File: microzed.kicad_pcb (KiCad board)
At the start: 10 copper layers, 19 x 19 mm, 329 parts, among them IC1 XC7Z020-1CLG484C, IC2 RTL8211E-VL-CG, J1 640456-3, J2 10104111-0001LF, J3 L829-1J1T-43, J4 Micro_SD_Card_Det_Hirose_DM3AT, J5 10104111-0001LF, J6 BSH-090-01-X-D-A, J7 BSH-090-01-X-D-A, Q1 MMBT3904, Q2 MMBT3904, SW1 SW_Push, U1 TLV62130RGTR, U10 MT41K256M16TW, U11 MT25QL128ABA8E12-1SIT, U12 USB3320C-EZK, U13 ASDMB-24.000MHZ-LC-T, U14 ASDMB-25.000MHZ-LC-T, U15 TXS02612RTWR, U16 CP2104-F03-GM, U2 TLV62130RGTR, U3 TLV62130RGTR, U4 TLV62130RGTR, U5 TLV62130RGTR, U6 ASDMB-33.333MHZ-LC-T, U7 TPS51206DSQR, U8 REF3012, U9 MT41K256M16TW

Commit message: add zone for GND
Signed-off-by: Yi Qingliang <niqingliang2003@gmail.com>
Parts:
- moved R19 0.09 mm to (-37.9, 23.4)
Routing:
- net GND: track 11.9 -> 3.14 mm
- net Net-(L4-Pad1): track 3.99 -> 0.00 mm
- net V3V3: track 6.68 -> 9.95 mm, vias 3 -> 2
- net /pwrcvt/PG_1V35: track 0.00 -> 1.85 mm, vias 0 -> 1
- net (no net): vias 0 -> 1
- added copper zone on In1.Cu.GND, net GND
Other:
- board size 19 x 19 mm -> 20.3 x 19 mm
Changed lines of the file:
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@@
     (thickness 1.6)
     (drawings 4)
-    (tracks 57)
+    (tracks 41)
     (zones 0)
     (modules 329)
@@
   (layers
     (0 F.Cu signal)
-    (1 In1.Cu power)
-    (2 In2.Cu signal)
-    (3 In3.Cu signal)
-    (4 In4.Cu power)
-    (5 In5.Cu power)
-    (6 In6.Cu signal)
-    (7 In7.Cu signal)
-    (8 In8.Cu power)
+    (1 In1.Cu.GND power)
+    (2 In2.Cu.signal signal)
+    (3 In3.Cu.signal signal)
+    (4 In4.Cu.VDD power)
+    (5 In5.Cu.GND power)
+    (6 In6.Cu.signal signal)
+    (7 In7.Cu.signal signal)
+    (8 In8.Cu.VCC power)
     (31 B.Cu signal)
     (32 B.Adhes user)
@@
     (trace_clearance 0.2)
     (zone_clearance 0.508)
-    (zone_45_only no)
+    (zone_45_only yes)
     (trace_min 0.2)
     (via_size 0.8)
@@
   )
   (module Resistor_SMD:R_0402_1005Metric (layer F.Cu)
-    (at -37.823 23.368)
+    (at -37.9095 23.368)
     (descr "Resistor SMD 0402 (1005 Metric), square (rectangular) end terminal, IPC_7351 nominal, (Body size source: http://www.tortai-tech.com/upload/download/2011102023233369053.pdf), generated with kicad-footprint-generator")
     (tags resistor)
@@
     )
   )
-  (gr_line (start -33.655 15.24) (end -33.655 34.29) (layer Edge.Cuts) (width 0.05))
-  (gr_line (start -52.705 15.24) (end -33.655 15.24) (layer Edge.Cuts) (width 0.05))
-  (gr_line (start -52.705 34.29) (end -52.705 15.24) (layer Edge.Cuts) (width 0.05))
-  (gr_line (start -33.655 34.29) (end -52.705 34.29) (layer Edge.Cuts) (width 0.05))
+  (gr_line (start -33.02 15.24) (end -33.02 34.29) (layer Edge.Cuts) (width 0.05))
+  (gr_line (start -53.34 15.24) (end -33.02 15.24) (layer Edge.Cuts) (width 0.05))
+  (gr_line (start -53.34 34.29) (end -53.34 15.24) (layer Edge.Cuts) (width 0.05))
+  (gr_line (start -33.02 34.29) (end -53.34 34.29) (layer Edge.Cuts) (width 0.05))
+  (via (at -41.91 25.908) (size 0.5) (drill 0.3) (layers F.Cu B.Cu) (net 0))
+  (via (at -39.37 29.21) (size 0.5) (drill 0.3) (layers F.Cu B.Cu) (net 9))
   (via (at -46.482 21.336) (size 0.5) (drill 0.3) (layers F.Cu B.Cu) (net 1))
   (via (at -47.498 22.352) (size 0.5) (drill 0.3) (layers F.Cu B.Cu) (net 1))
   (via (at -37.338 22.352) (size 0.5) (drill 0.3) (layers F.Cu B.Cu) (net 1))
-  (via (at -39.878 22.86) (size 0.5) (drill 0.3) (layers F.Cu B.Cu) (net 350))
-  (via (at -43.688 24.892) (size 0.5) (drill 0.3) (layers F.Cu B.Cu) (net 1))
-  (via (at -43.18 24.384) (size 0.5) (drill 0.3) (layers F.Cu B.Cu) (net 1))
+  (via (at -43.688 24.765) (size 0.5) (drill 0.3) (layers F.Cu B.Cu) (net 1))
+  (via (at -43.18 24.301) (size 0.5) (drill 0.3) (layers F.Cu B.Cu) (net 1))
   (via (at -43.688 23.876) (size 0.5) (drill 0.3) (layers F.Cu B.Cu) (net 1))
   (via (at -42.672 23.876) (size 0.5) (drill 0.3) (layers F.Cu B.Cu) (net 1))
-  (via (at -42.672 24.892) (size 0.5) (drill 0.3) (layers F.Cu B.Cu) (net 1))
-  (segment (start -42.43 25.08) (end -42.545 24.965) (width 0.25) (layer F.Cu) (net 1))
-  (segment (start -42.43 25.5925) (end -42.43 25.08) (width 0.25) (layer F.Cu) (net 1))
-  (segment (start -42.93 25.5925) (end -42.93 25.015) (width 0.25) (layer F.Cu) (net 1))
-  (segment (start -43.43 22.6675) (end -43.43 23.88) (width 0.25) (layer F.Cu) (net 1))
-  (segment (start -42.93 22.6675) (end -42.93 23.88) (width 0.25) (layer F.Cu) (net 1))
-  (segment (start -44.473 21.336) (end -43.411 21.336) (width 0.25) (layer F.Cu) (net 1))
-  (segment (start -43.43 22.9215) (end -43.43 21.594) (width 0.25) (layer F.Cu) (net 1))
-  (segment (start -43.93 22.9215) (end -43.93 23.434) (width 0.25) (layer F.Cu) (net 1))
+  (via (at -42.672 24.765) (size 0.5) (drill 0.3) (layers F.Cu B.Cu) (net 1))
   (segment (start -37.338 23.368) (end -37.338 22.352) (width 0.25) (layer F.Cu) (net 1))
   (segment (start -46.482 22.398) (end -46.482 21.336) (width 0.25) (layer F.Cu) (net 1))
@@
   (segment (start -46.482 22.398) (end -47.452 22.398) (width 0.25) (layer F.Cu) (net 1))
   (segment (start -42.93 27.9185) (end -42.9515 27.94) (width 0.25) (layer F.Cu) (net 1))
-  (segment (start -42.93 25.7635) (end -42.93 27.9185) (width 0.25) (layer F.Cu) (net 1))
   (segment (start -45.799 24.051) (end -46.482 23.368) (width 0.25) (layer F.Cu) (net 2))
   (segment (start -44.6425 24.051) (end -45.799 24.051) (width 0.25) (layer F.Cu) (net 2))
@@
   (via (at -39.37 21.336) (size 0.5) (drill 0.3) (layers F.Cu B.Cu) (net 9))
   (segment (start -40.432 21.336) (end -38.354 21.336) (width 0.25) (layer F.Cu) (net 9))
-  (segment (start -39.129 27.94) (end -38.735 27.546) (width 0.25) (layer F.Cu) (net 9))
-  (segment (start -41.3765 27.94) (end -40.132 27.94) (width 0.25) (layer F.Cu) (net 9))
-  (segment (start -40.132 27.94) (end -40.132 27.94) (width 0.25) (layer F.Cu) (net 9))
-  (segment (start -40.132 27.94) (end -40.132 27.94) (width 0.25) (layer F.Cu) (net 9))
-  (segment (start -40.132 27.94) (end -39.129 27.94) (width 0.25) (layer F.Cu) (net 9))
-  (via (at -40.894 29.21) (size 0.5) (drill 0.3) (layers F.Cu B.Cu) (net 9))
-  (via (at -44.45 26.924) (size 0.5) (drill 0.3) (layers F.Cu B.Cu) (net 9))
-  (segment (start -43.43 26.276) (end -43.824 26.67) (width 0.25) (layer F.Cu) (net 9))
-  (segment (start -43.43 25.7635) (end -43.43 26.276) (width 0.25) (layer F.Cu) (net 9))
-  (segment (start -43.824 26.67) (end -44.196 26.67) (width 0.25) (layer F.Cu) (net 9))
-  (segment (start -44.196 26.67) (end -44.45 26.924) (width 0.25) (layer F.Cu) (net 9))
-  (segment (start -40.652 23.634) (end -39.878 22.86) (width 0.25) (layer F.Cu) (net 350))
-  (segment (start -41.7175 23.634) (end -40.652 23.634) (width 0.25) (layer F.Cu) (net 350))
-  (segment (start -39.878 22.86) (end -38.354 22.86) (width 0.25) (layer F.Cu) (net 350))
+  (segment (start -39.37 29.21) (end -39.37 21.336) (width 0.25) (layer In2.Cu.signal) (net 9))
+  (via (at -40.132 22.86) (size 0.5) (drill 0.3) (layers F.Cu B.Cu) (net 350))
   (segment (start -38.354 22.306) (end -38.354 22.86) (width 0.25) (layer F.Cu) (net 350))
   (segment (start -38.354 22.86) (end -38.354 23.114) (width 0.25) (layer F.Cu) (net 350))
-  (segment (start -38.83 25.051) (end -38.735 25.146) (width 0.25) (layer F.Cu) (net 422))
-  (segment (start -41.7175 25.051) (end -38.83 25.051) (width 0.25) (layer F.Cu) (net 422))
-  (segment (start -41.7175 24.551) (end -41.7175 25.051) (width 0.25) (layer F.Cu) (net 422))
-  (segment (start -41.7175 24.551) (end -41.7175 24.08401) (width 0.25) (layer F.Cu) (net 422))
+  (segment (start -40.823 23.551) (end -40.132 22.86) (width 0.25) (layer F.Cu) (net 350))
+  (segment (start -41.7175 23.551) (end -40.823 23.551) (width 0.25) (layer F.Cu) (net 350))
+  (segment (start -40.132 22.86) (end -38.354 22.86) (width 0.25) (layer F.Cu) (net 350))
   (segment (start -42.441 21.336) (end -41.402 21.336) (width 0.25) (layer F.Cu) (net 434))
   (segment (start -42.43 22.9215) (end -42.43 21.602) (width 0.25) (layer F.Cu) (net 434))
+  (segment (start -44.155 25.7635) (end -44.2995 25.908) (width 0.25) (layer F.Cu) (net 436))
+  (segment (start -43.93 25.7635) (end -44.155 25.7635) (width 0.25) (layer F.Cu) (net 436))
+  (segment (start -44.2995 25.908) (end -45.72 25.908) (width 0.25) (layer F.Cu) (net 436))
+  (segment (start -45.72 25.908) (end -45.72 25.908) (width 0.25) (layer F.Cu) (net 436))
+  (via (at -45.72 25.908) (size 0.5) (drill 0.3) (layers F.Cu B.Cu) (net 436))
   (segment (start -45.443 21.756) (end -45.443 21.336) (width 0.25) (layer F.Cu) (net 485))
   (segment (start -45.443 22.995) (end -45.443 21.756) (width 0.25) (layer F.Cu) (net 485))
   (segment (start -44.887 23.551) (end -45.443 22.995) (width 0.25) (layer F.Cu) (net 485))
   (segment (start -44.6425 23.551) (end -44.887 23.551) (width 0.25) (layer F.Cu) (net 485))
+  (zone (net 1) (net_name GND) (layer In1.Cu.GND) (hatch edge 0.508)
+    (connect_pads (clearance 0.508))
+    (min_thickness 0.254)
+    (fill yes (arc_segments 32) (thermal_gap 0.508) (thermal_bridge_width 0.508))
+    (polygon
+      (pts
+        (xy -33.02 15.24) (xy -53.34 15.24) (xy -53.34 34.29) (xy -33.02 34.29)
+      )
+    )
+  )
 )

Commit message: 3.3V power
Signed-off-by: Yi Qingliang <niqingliang2003@gmail.com>
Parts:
- R18, R19: moved to B.Cu
- moved LED1 6.71 mm to (-35.6, 22.1), turned to 90 degrees
- moved R22 5.46 mm to (-37.3, 21.3), turned to 180 degrees
- moved R19 4.23 mm to (-42.0, 22.4), turned to 180 degrees
- moved R18 2.03 mm to (-40.4, 21.8)
- moved C14 0.67 mm to (-46.6, 22.2)
- moved L4 0.51 mm to (-38.7, 25.8)
- moved IC1 0.45 mm to (131.2, 102.9)
- moved C13 0.21 mm to (-47.0, 26.0)
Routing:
- net V3V3: track 9.95 -> 23.2 mm, vias 2 -> 3
- net VIN: track 7.02 -> 4.08 mm, vias 0 -> 3
- net Net-(LED1-Pad2): track 0.00 -> 1.30 mm
- net GND: track 3.14 -> 2.49 mm, vias 8 -> 15
- net PG_MODULE: track 4.46 -> 4.97 mm
- net (no net): vias 1 -> 0
- added copper zone on F.Cu, net GND
- added copper zone on F.Cu, net Net-(L4-Pad1)
- added copper zone on B.Cu, net PG_MODULE
- added copper zone on F.Cu, net V3V3
- added copper zone on F.Cu, net VIN
- added copper zone on In8.Cu.VCC, net VIN

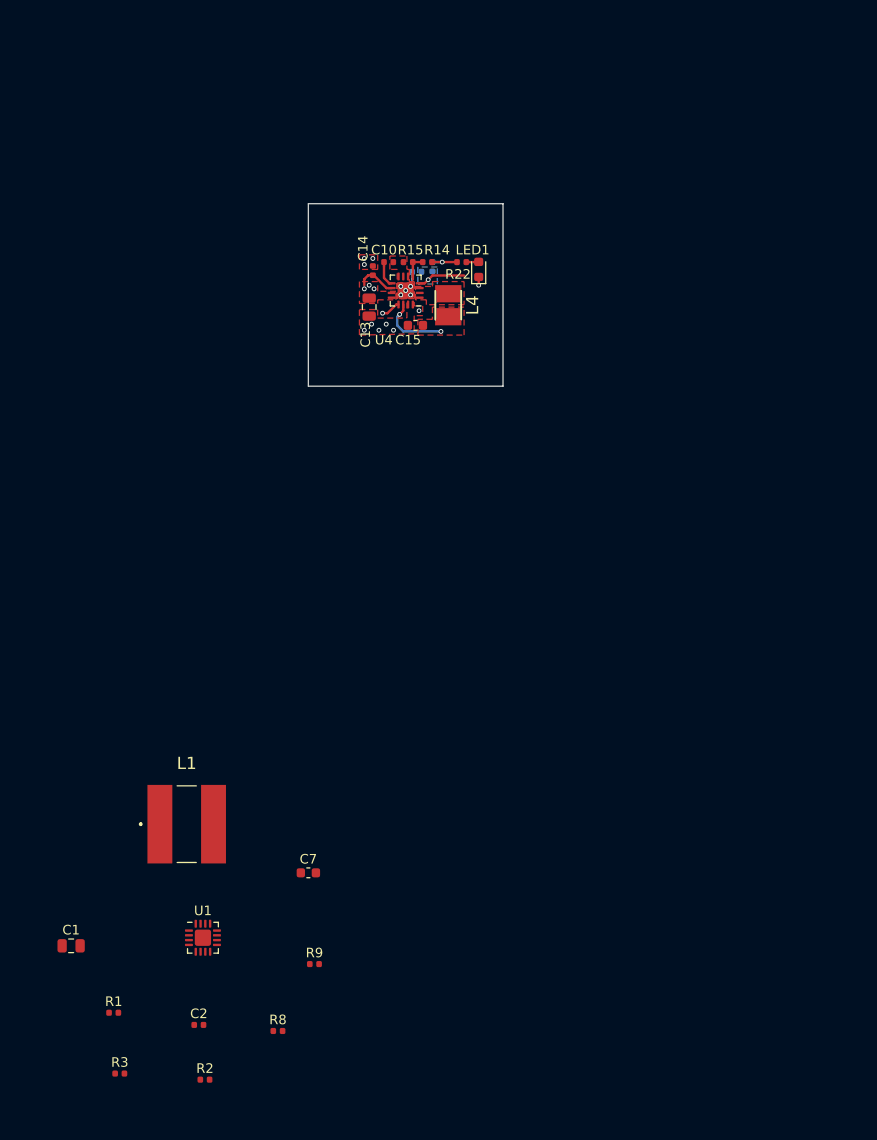
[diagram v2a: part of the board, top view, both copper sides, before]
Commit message: pcb: remove filled zone
Signed-off-by: Yi Qingliang <niqingliang2003@gmail.com>
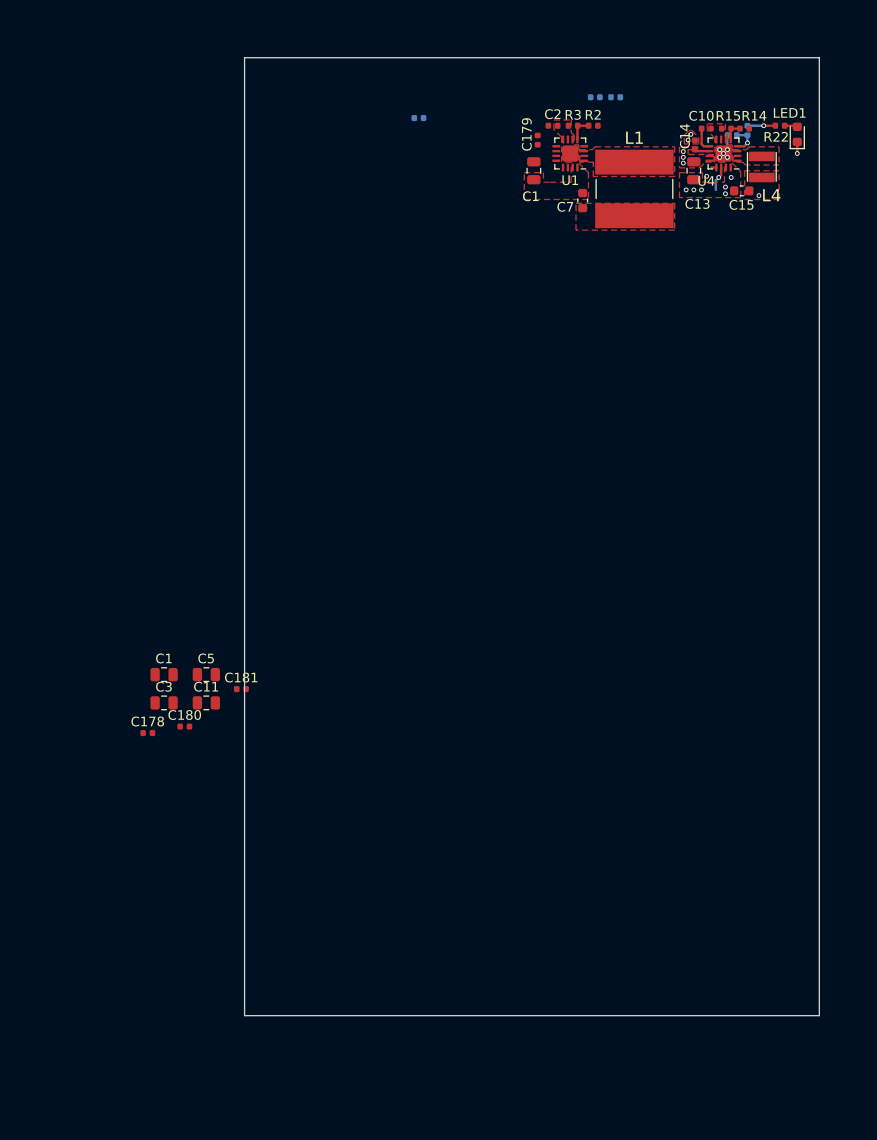
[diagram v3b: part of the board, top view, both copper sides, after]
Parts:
- removed the C1 at (-78.1, 92.7)
- added C1: 10µF, Capacitor_SMD:C_0805_2012Metric, F.Cu at (-68.4, 64.4)
- added C1: 10µF, Capacitor_SMD:C_0805_2012Metric, F.Cu at (-29.8, 11.8)
- added C11: 10µF, Capacitor_SMD:C_0805_2012Metric, F.Cu at (-64.0, 67.3)
- added C178: 0.1µF, Capacitor_SMD:C_0402_1005Metric, F.Cu at (-70.1, 70.5)
- added C179: 0.1µF, Capacitor_SMD:C_0402_1005Metric, F.Cu at (-29.4, 8.60)
- added C180: 0.1µF, Capacitor_SMD:C_0402_1005Metric, F.Cu at (-66.2, 69.8)
- added C181: 0.1µF, Capacitor_SMD:C_0402_1005Metric, F.Cu at (-60.3, 65.9)
- added C3: 10µF, Capacitor_SMD:C_0805_2012Metric, F.Cu at (-68.4, 67.3)
- added C5: 10µF, Capacitor_SMD:C_0805_2012Metric, F.Cu at (-64.0, 64.4)
- R1, R8, R9: moved to B.Cu
- moved R3 109.7 mm to (-25.7, 7.10), turned to 180 degrees
- moved R2 107.5 mm to (-23.6, 7.10), turned to 180 degrees
- moved R8 102.9 mm to (-23.4, 4.12)
- moved C2 100.9 mm to (-27.8, 7.10)
- moved R1 98.7 mm to (-41.8, 6.30)
- moved R9 95.8 mm to (-21.3, 4.12)
- moved U1 90.4 mm to (-26.0, 10.0), turned to 180 degrees
- moved L1 81.1 mm to (-19.3, 13.7), turned to 270 degrees
- moved C7 75.8 mm to (-24.7, 14.9), turned to 90 degrees
- moved C15 36.8 mm to (-8.10, 13.9)
- moved C13 36.8 mm to (-13.1, 11.8)
- moved R22 36.2 mm to (-4.10, 7.10)
- moved U4 36.1 mm to (-10.0, 10.0)
- moved LED1 36.1 mm to (-2.30, 8.00)
- moved C14 36.1 mm to (-13.0, 9.10)
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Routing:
- net V3V3: track 23.2 -> 17.1 mm
- net Net-(R2-Pad2): track 0.00 -> 2.58 mm
- net VIN: track 4.08 -> 1.56 mm
- net PG_MODULE: track 4.97 -> 3.12 mm
- net /pwrcvt/PG_1V35: track 2.03 -> 0.51 mm
- net GND: track 2.49 -> 2.72 mm, vias 15 -> 14
- added copper zone on F.Cu, net Net-(L1-Pad1)
- added copper zone on F.Cu, net VCCBRAM
- removed copper zone on B.Cu, net PG_MODULE
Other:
- board size 20.3 x 19 mm -> 60 x 100 mm
- rule pad_to_mask_clearance: 0.051 -> 0.05

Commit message: pcb: power init done
Signed-off-by: Yi Qingliang <niqingliang2003@gmail.com>
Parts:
- removed the C1 at (-68.4, 64.4)
- removed the C1 at (-29.8, 11.8)
- removed the C11 at (-64.0, 67.3)
- removed the C11 at (-95.9, 149.9)
- removed the C3 at (-76.8, 207.0)
- added C1: 10µF, Capacitor_SMD:C_0805_2012Metric, F.Cu at (-28.3, 11.9)
- added C11: 10µF, Capacitor_SMD:C_0805_2012Metric, F.Cu at (-38.1, 11.9)
- R10, R11, R20, R21: moved to B.Cu
- moved C5 429.0 mm to (288.6, 308.7)
- moved C181 429.0 mm to (292.3, 310.2)
- moved R5 227.8 mm to (-44.5, 7.40), turned to 180 degrees
- moved R4 222.8 mm to (-42.6, 7.40), turned to 180 degrees
- moved R11 222.6 mm to (-44.5, 7.40), turned to 180 degrees
- moved C4 218.9 mm to (-46.4, 7.40)
- moved L2 213.3 mm to (-40.9, 11.5), turned to 180 degrees
- moved R10 213.2 mm to (-42.6, 7.40), turned to 180 degrees
- moved U2 203.3 mm to (-44.8, 10.0), turned to 180 degrees
- moved C8 196.5 mm to (-44.2, 13.4), turned to 180 degrees
- moved C12 159.2 mm to (-36.6, 7.40)
- moved R17 153.2 mm to (-34.7, 7.40), turned to 180 degrees
- moved L5 151.6 mm to (-31.1, 11.5), turned to 180 degrees
- moved R21 149.8 mm to (-34.7, 7.40), turned to 180 degrees
- moved R16 146.1 mm to (-32.8, 7.40), turned to 180 degrees
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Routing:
- net /pwrcvt/PG_1V: track 0.00 -> 33.7 mm, vias 0 -> 2
- net /pwrcvt/PG_1V35: track 0.51 -> 27.6 mm, vias 1 -> 2
- net VCCBRAM: track 0.00 -> 14.1 mm, vias 0 -> 7
- net VCCO_DDR: track 0.00 -> 12.7 mm, vias 0 -> 7
- net PWR_B501: track 0.00 -> 12.1 mm, vias 0 -> 6
- net PG_1V8: track 0.00 -> 11.9 mm, vias 0 -> 2
- net VIN: track 1.56 -> 11.9 mm, vias 3 -> 12
- net GND: track 2.72 -> 12.1 mm, vias 14 -> 45
- net V3V3: track 17.1 -> 10.7 mm, vias 3 -> 7
- net PWR_EN: track 0.00 -> 2.25 mm, vias 0 -> 1
- net Net-(C12-Pad1): track 0.00 -> 2.11 mm
- net Net-(C2-Pad1): track 0.00 -> 2.11 mm
- net Net-(C4-Pad1): track 0.00 -> 2.11 mm
- net Net-(R16-Pad2): track 0.00 -> 2.03 mm
- net Net-(R4-Pad2): track 0.00 -> 2.03 mm
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- added copper zone on F.Cu, net Net-(L2-Pad1)
- added copper zone on F.Cu, net Net-(L5-Pad1)
- added copper zone on F.Cu, net PWR_B501
- added copper zone on F.Cu, net VCCO_DDR

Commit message: pcb: start memory
Signed-off-by: Yi Qingliang <niqingliang2003@gmail.com>
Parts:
- moved J4 657.7 mm to (-274.4, 273.8)
- moved C169 656.2 mm to (-260.0, 274.3)
- moved C170 656.2 mm to (-256.6, 271.9)
- moved R96 656.2 mm to (-256.4, 268.1)
- moved R97 656.2 mm to (-262.7, 274.4)
- moved R98 656.2 mm to (-256.4, 270.0)
- moved R99 656.2 mm to (-253.5, 268.1)
- moved C168 656.2 mm to (-263.0, 276.3)
- moved C171 656.2 mm to (-263.0, 278.0)
- moved U15 656.2 mm to (-286.7, 261.5)
- moved D1 548.7 mm to (-142.0, 259.0)
- moved R73 545.2 mm to (-118.8, 255.6)
- moved J2 545.2 mm to (-124.5, 263.9)
- moved C145 518.4 mm to (-130.7, 237.6)
- moved C141 518.4 mm to (-154.8, 253.5)
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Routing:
- net GND: track 12.1 -> 16.4 mm
- net V3V3: track 10.7 -> 12.3 mm
- net PWR_B501: track 12.1 -> 12.3 mm, vias 6 -> 7
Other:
- board size 60 x 100 mm -> 50 x 100 mm
